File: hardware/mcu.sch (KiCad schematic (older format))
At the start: 17 parts

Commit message: przeniosiono do folderu hardware
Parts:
- added SW? (x2): SW_Push, symbol Switch:SW_Push
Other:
- note added: "or dip swichtes?\n"
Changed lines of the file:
@@
 Text Label 4900 4900 0    50   ~ 0
 POTSHDN
+$Comp
+L Switch:SW_Push SW?
+U 1 1 5D80555F
+P 8400 3600
+F 0 "SW?" H 8400 3885 50  0000 C CNN
+F 1 "SW_Push" H 8400 3794 50  0000 C CNN
+F 2 "" H 8400 3800 50  0001 C CNN
+F 3 "~" H 8400 3800 50  0001 C CNN
+	1    8400 3600
+	1    0    0    -1
+$EndComp
+$Comp
+L Switch:SW_Push SW?
+U 1 1 5D805DAF
+P 8400 4000
+F 0 "SW?" H 8400 4285 50  0000 C CNN
+F 1 "SW_Push" H 8400 4194 50  0000 C CNN
+F 2 "" H 8400 4200 50  0001 C CNN
+F 3 "~" H 8400 4200 50  0001 C CNN
+	1    8400 4000
+	1    0    0    -1
+$EndComp
+Text Notes 8100 3250 0    50   ~ 0
+or dip swichtes?\n
+Wire Notes Line
+	9200 4750 9200 2800
+Wire Notes Line
+	9200 2800 7800 2800
+Wire Notes Line
+	7800 2800 7800 4750
+Wire Notes Line
+	7800 4750 9200 4750
 $EndSCHEMATC

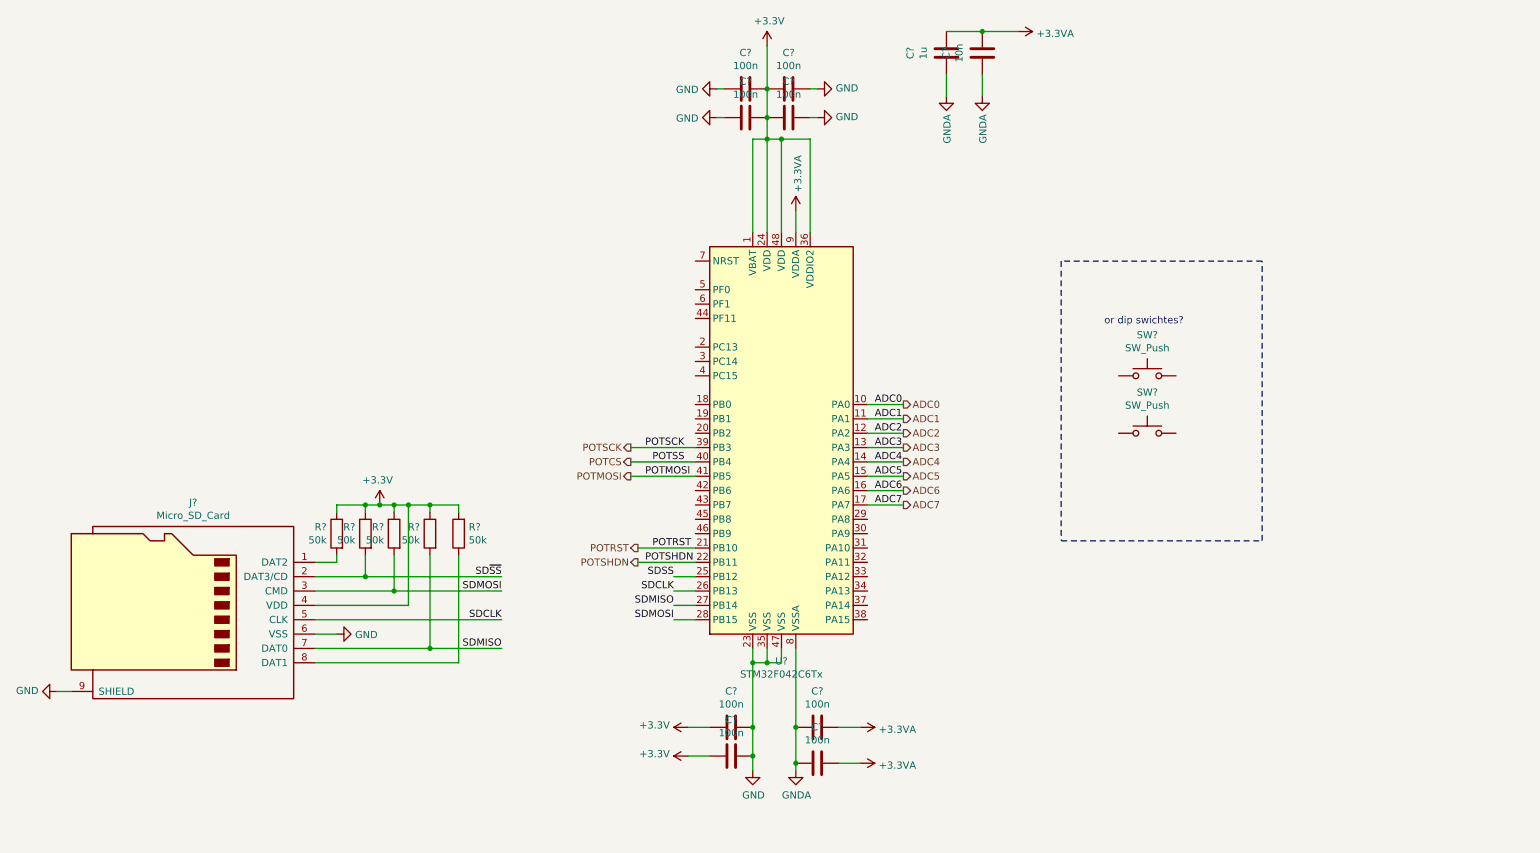
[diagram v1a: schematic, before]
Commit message: dodano wyjscie programatora, przyciski ustalono wysjcie i2c, dodany plik CubeMX z pinouterm
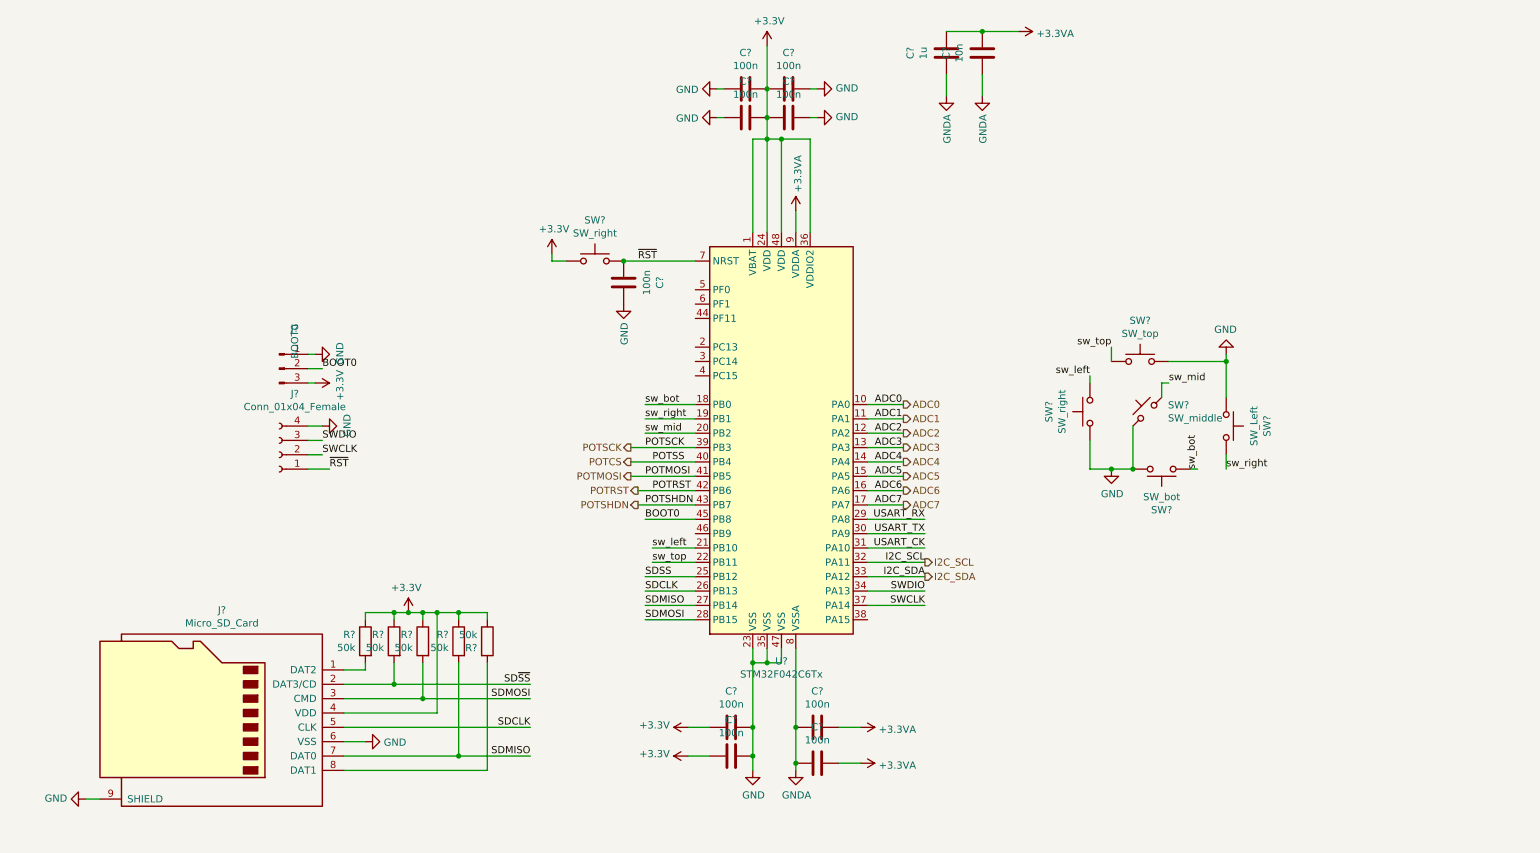
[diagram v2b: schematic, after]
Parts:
- added C?: 100n, symbol Device:C
- added J?: BOOT0, symbol Connector:Conn_01x03_Male
- added J?: Conn_01x04_Female, symbol Connector:Conn_01x04_Female
- added SW?: SW_top, symbol Switch:SW_Push
- added SW?: SW_bot, symbol Switch:SW_Push
- added SW?: SW_middle, symbol Switch:SW_Push_45deg
- added SW?: SW_right, symbol Switch:SW_Push
- SW?: value SW_Push -> SW_Left
- SW?: value SW_Push -> SW_right
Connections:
- net +3V3: now also R?.1, J?.3 (Pin_3), SW?.1; no longer R?.2
- net GND: now also SW?.1, SW?.1, C?.1, J?.1 (Pin_1), J?.4 (Pin_4), SW?.1, SW?.2, SW?.2
- net POTRST: now also U?.42 (PB6); no longer U?.21 (PB10)
- net POTSHDN: now also U?.43 (PB7); no longer U?.22 (PB11)
- net at J?.8 (DAT1): now also R?.2; no longer R?.1
- net sw_bot: now reaches U?.18 (PB0)
- net sw_bot: now also SW?.1
- net sw_right: now reaches U?.19 (PB1)
- net sw_right: now also SW?.2
- net sw_mid: now reaches U?.20 (PB2)
- net sw_mid: now also SW?.2
- net USART_RX: now reaches U?.29 (PA8)
- net USART_TX: now reaches U?.30 (PA9)
- net USART_CK: now reaches U?.31 (PA10)
- net I2C_SCL: now reaches U?.32 (PA11)
- net I2C_SDA: now reaches U?.33 (PA12)
- net SWDIO: now reaches U?.34 (PA13)
- net SWDIO: now also J?.3 (Pin_3)
- net SWCLK: now reaches U?.37 (PA14)
- net SWCLK: now also J?.2 (Pin_2)
- net BOOT0: now reaches U?.45 (PB8)
- net BOOT0: now also J?.2 (Pin_2)
- net ~RST: now reaches U?.7 (NRST)
- net ~RST: now also C?.2, J?.1 (Pin_1), SW?.2
- net sw_left: now reaches SW?.2
- net sw_left: now also U?.21 (PB10)
- new net sw_top: SW?.1, U?.22 (PB11)
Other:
- note removed: "or dip swichtes?\n"
- moved on the sheet: J?, R?, SW?

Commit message: DRC przechodzi dorzucone złącze do wyświetlacza na i2c oraz jeden push button
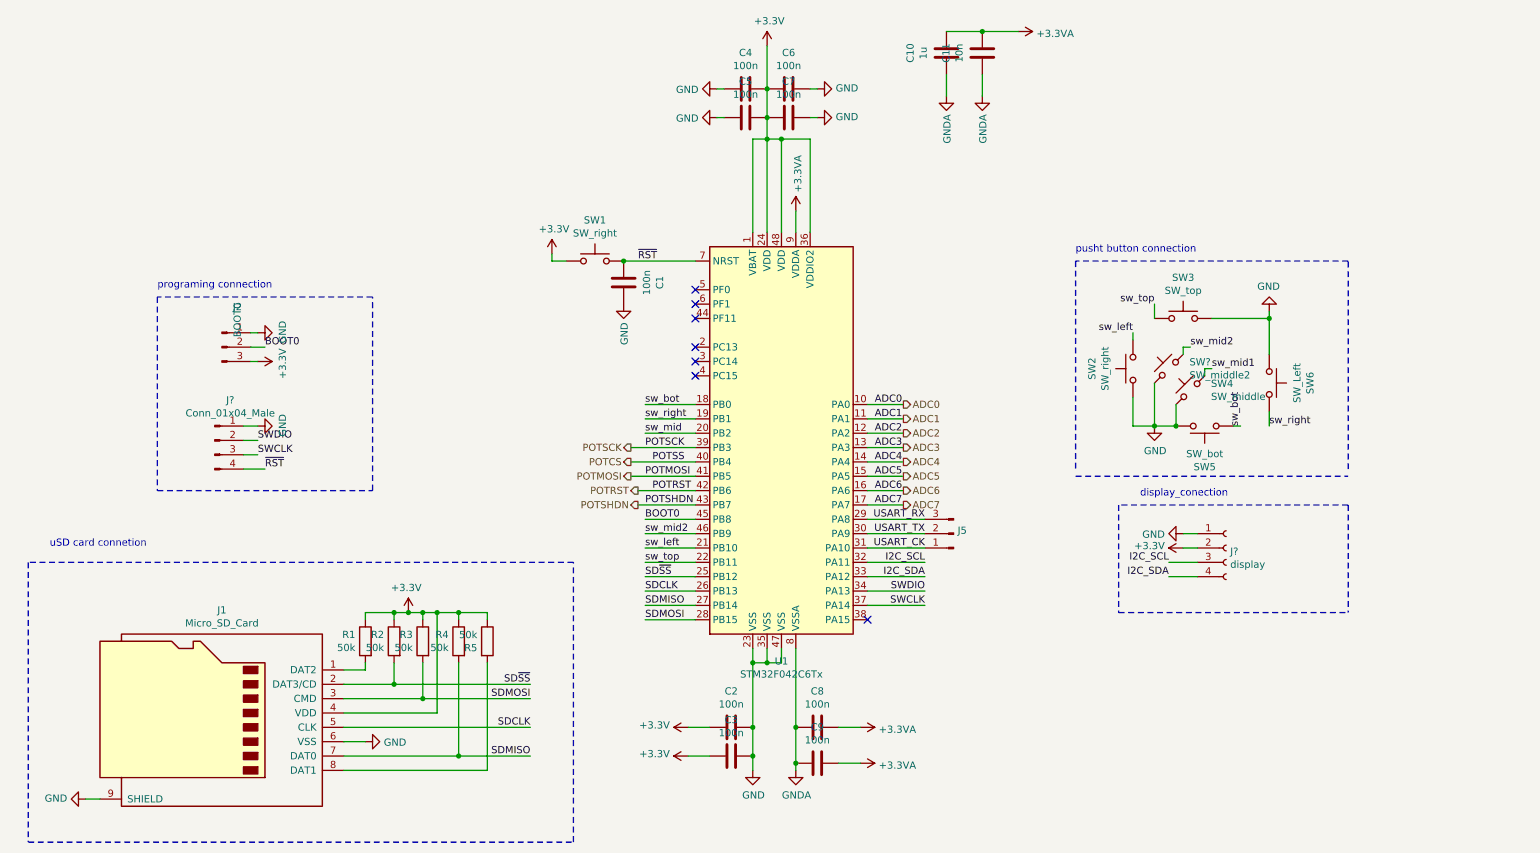
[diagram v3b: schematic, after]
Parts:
- removed J?: Conn_01x04_Female, symbol Connector:Conn_01x04_Female
- added J5: Conn_01x03_Male, symbol Connector:Conn_01x03_Male
- added J?: Conn_01x04_Male, symbol Connector:Conn_01x04_Male
- added J?: display, symbol Connector:Conn_01x04_Female
- added SW?: SW_middle2, symbol Switch:SW_Push_45deg
- gave numbers to parts that had none: 25
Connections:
- net SDSS is gone; now on net SD~SS: U1.25 (PB12)
- net +3V3: now also J?.2 (Pin_2)
- net GND: now also J?.1 (Pin_1), J?.1 (Pin_1), SW?.1
- net I2C_SCL: now also J?.3 (Pin_3)
- net I2C_SDA: now also J?.4 (Pin_4)
- net SWCLK: now also J?.3 (Pin_3)
- net SWDIO: now also J?.2 (Pin_2)
- net USART_CK: now also J5.1 (Pin_1)
- net USART_RX: now also J5.3 (Pin_3)
- net USART_TX: now also J5.2 (Pin_2)
- net sw_mid: no longer SW4.2
- net ~RST: now also J?.4 (Pin_4)
- net sw_mid2: now reaches U1.46 (PB9)
- net sw_mid2: now also SW?.2
- new net sw_mid1: SW4.2
- no-connect marks 0 -> 7
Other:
- note added: "display_conection"
- note added: "programing connection\n"
- note added: "pusht button connection"
- note added: "uSD card connetion\n"
- moved on the sheet: J2, SW2, SW3, SW4, SW5, SW6

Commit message: przypisano footprinty
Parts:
- C1, C10, C11, C2, C3, C4, C5, C6, C7, C8, C9: footprint (none) -> Capacitor_SMD:C_0603_1608Metric_Pad1.05x0.95mm_HandSolder
- J1: footprint (none) -> Connector_Card:microSD_HC_Hirose_DM3AT-SF-PEJM5
- J2: footprint (none) -> Connector_PinHeader_2.54mm:PinHeader_1x03_P2.54mm_Vertical
- J3: renamed from J?; footprint (none) -> Connector_PinHeader_2.54mm:PinHeader_1x04_P2.54mm_Vertical
- J5: footprint (none) -> Connector_PinHeader_2.54mm:PinHeader_1x03_P2.54mm_Horizontal
- J6: renamed from J?; footprint (none) -> Connector_PinSocket_2.54mm:PinSocket_1x04_P2.54mm_Vertical
- R1, R2, R3, R4, R5: footprint (none) -> Resistor_SMD:R_0603_1608Metric_Pad1.05x0.95mm_HandSolder
- SW1, SW2, SW3, SW4, SW5, SW6: footprint (none) -> Button_Switch_SMD:SW_Push_1P1T_NO_CK_KSC6xxJ
- SW7: renamed from SW?; footprint (none) -> Button_Switch_SMD:SW_Push_1P1T_NO_CK_KSC6xxJ
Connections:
- net sw_mid is gone; now on net sw_mid1: U1.20 (PB2)
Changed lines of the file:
@@
 F 0 "C2" V 5248 6050 50  0000 C CNN
 F 1 "100n" V 5339 6050 50  0000 C CNN
-F 2 "" H 5538 5900 50  0001 C CNN
+F 2 "Capacitor_SMD:C_0603_1608Metric_Pad1.05x0.95mm_HandSolder" H 5538 5900 50  0001 C CNN
 F 3 "~" H 5500 6050 50  0001 C CNN
 	1    5500 6050
@@
 F 0 "C6" V 5648 1600 50  0000 C CNN
 F 1 "100n" V 5739 1600 50  0000 C CNN
-F 2 "" H 5938 1450 50  0001 C CNN
+F 2 "Capacitor_SMD:C_0603_1608Metric_Pad1.05x0.95mm_HandSolder" H 5938 1450 50  0001 C CNN
 F 3 "~" H 5900 1600 50  0001 C CNN
 	1    5900 1600
@@
 F 0 "C7" V 5648 1800 50  0000 C CNN
 F 1 "100n" V 5739 1800 50  0000 C CNN
-F 2 "" H 5938 1650 50  0001 C CNN
+F 2 "Capacitor_SMD:C_0603_1608Metric_Pad1.05x0.95mm_HandSolder" H 5938 1650 50  0001 C CNN
 F 3 "~" H 5900 1800 50  0001 C CNN
 	1    5900 1800
@@
 F 0 "C4" V 5348 1600 50  0000 C CNN
 F 1 "100n" V 5439 1600 50  0000 C CNN
-F 2 "" H 5638 1450 50  0001 C CNN
+F 2 "Capacitor_SMD:C_0603_1608Metric_Pad1.05x0.95mm_HandSolder" H 5638 1450 50  0001 C CNN
 F 3 "~" H 5600 1600 50  0001 C CNN
 	1    5600 1600
@@
 F 0 "C5" V 5348 1800 50  0000 C CNN
 F 1 "100n" V 5439 1800 50  0000 C CNN
-F 2 "" H 5638 1650 50  0001 C CNN
+F 2 "Capacitor_SMD:C_0603_1608Metric_Pad1.05x0.95mm_HandSolder" H 5638 1650 50  0001 C CNN
 F 3 "~" H 5600 1800 50  0001 C CNN
 	1    5600 1800
@@
 F 0 "C11" V 6998 1350 50  0000 C CNN
 F 1 "10n" V 7089 1350 50  0000 C CNN
-F 2 "" H 7288 1200 50  0001 C CNN
+F 2 "Capacitor_SMD:C_0603_1608Metric_Pad1.05x0.95mm_HandSolder" H 7288 1200 50  0001 C CNN
 F 3 "~" H 7250 1350 50  0001 C CNN
 	1    7250 1350
@@
 F 0 "C10" V 6748 1350 50  0000 C CNN
 F 1 "1u" V 6839 1350 50  0000 C CNN
-F 2 "" H 7038 1200 50  0001 C CNN
+F 2 "Capacitor_SMD:C_0603_1608Metric_Pad1.05x0.95mm_HandSolder" H 7038 1200 50  0001 C CNN
 F 3 "~" H 7000 1350 50  0001 C CNN
 	1    7000 1350
@@
 F 0 "J1" H 1850 6667 50  0000 C CNN
 F 1 "Micro_SD_Card" H 1850 6576 50  0000 C CNN
-F 2 "" H 3050 6250 50  0001 C CNN
-F 3 "http://katalog.we-online.de/em/datasheet/693072010801.pdf" H 1900 5950 50  0001 C CNN
+F 2 "Connector_Card:microSD_HC_Hirose_DM3AT-SF-PEJM5" H 3050 6250 50  0001 C CNN
+F 3 "https://www.tme.eu/pl/details/mcsp-q-08-a-sg/zlacza-do-kart/adam-tech/mcsp-q-08-a-sg-t-r/" H 1900 5950 50  0001 C CNN
 	1    1900 5950
 	-1   0    0    -1
@@
 F 0 "R1" H 3020 5496 50  0000 L CNN
 F 1 "50k" H 3020 5405 50  0000 L CNN
-F 2 "" V 2880 5450 50  0001 C CNN
+F 2 "Resistor_SMD:R_0603_1608Metric_Pad1.05x0.95mm_HandSolder" V 2880 5450 50  0001 C CNN
 F 3 "~" H 2950 5450 50  0001 C CNN
 	1    2950 5450
@@
 F 0 "R2" H 3220 5496 50  0000 L CNN
 F 1 "50k" H 3220 5405 50  0000 L CNN
-F 2 "" V 3080 5450 50  0001 C CNN
+F 2 "Resistor_SMD:R_0603_1608Metric_Pad1.05x0.95mm_HandSolder" V 3080 5450 50  0001 C CNN
 F 3 "~" H 3150 5450 50  0001 C CNN
 	1    3150 5450
@@
 F 0 "R3" H 3420 5496 50  0000 L CNN
 F 1 "50k" H 3420 5405 50  0000 L CNN
-F 2 "" V 3280 5450 50  0001 C CNN
+F 2 "Resistor_SMD:R_0603_1608Metric_Pad1.05x0.95mm_HandSolder" V 3280 5450 50  0001 C CNN
 F 3 "~" H 3350 5450 50  0001 C CNN
 	1    3350 5450
@@
 F 0 "R4" H 3670 5496 50  0000 L CNN
 F 1 "50k" H 3670 5405 50  0000 L CNN
-F 2 "" V 3530 5450 50  0001 C CNN
+F 2 "Resistor_SMD:R_0603_1608Metric_Pad1.05x0.95mm_HandSolder" V 3530 5450 50  0001 C CNN
 F 3 "~" H 3600 5450 50  0001 C CNN
 	1    3600 5450
@@
 F 0 "R5" H 3730 5404 50  0000 R CNN
 F 1 "50k" H 3730 5495 50  0000 R CNN
-F 2 "" V 3730 5450 50  0001 C CNN
+F 2 "Resistor_SMD:R_0603_1608Metric_Pad1.05x0.95mm_HandSolder" V 3730 5450 50  0001 C CNN
 F 3 "~" H 3800 5450 50  0001 C CNN
 	1    3800 5450
@@
 F 0 "C3" V 5248 6250 50  0000 C CNN
 F 1 "100n" V 5339 6250 50  0000 C CNN
-F 2 "" H 5538 6100 50  0001 C CNN
+F 2 "Capacitor_SMD:C_0603_1608Metric_Pad1.05x0.95mm_HandSolder" H 5538 6100 50  0001 C CNN
 F 3 "~" H 5500 6250 50  0001 C CNN
 	1    5500 6250
@@
 F 0 "C8" V 5848 6050 50  0000 C CNN
 F 1 "100n" V 5939 6050 50  0000 C CNN
-F 2 "" H 6138 5900 50  0001 C CNN
+F 2 "Capacitor_SMD:C_0603_1608Metric_Pad1.05x0.95mm_HandSolder" H 6138 5900 50  0001 C CNN
 F 3 "~" H 6100 6050 50  0001 C CNN
 	1    6100 6050
@@
 F 0 "C9" V 5848 6300 50  0000 C CNN
 F 1 "100n" V 5939 6300 50  0000 C CNN
-F 2 "" H 6138 6150 50  0001 C CNN
+F 2 "Capacitor_SMD:C_0603_1608Metric_Pad1.05x0.95mm_HandSolder" H 6138 6150 50  0001 C CNN
 F 3 "~" H 6100 6300 50  0001 C CNN
 	1    6100 6300
@@
 F 0 "SW6" H 9250 3935 50  0000 C CNN
 F 1 "SW_Left" H 9250 3844 50  0000 C CNN
-F 2 "" H 9250 3850 50  0001 C CNN
+F 2 "Button_Switch_SMD:SW_Push_1P1T_NO_CK_KSC6xxJ" H 9250 3850 50  0001 C CNN
 F 3 "~" H 9250 3850 50  0001 C CNN
 	1    9250 3650
@@
 F 0 "SW2" H 8300 3835 50  0000 C CNN
 F 1 "SW_right" H 8300 3744 50  0000 C CNN
-F 2 "" H 8300 3750 50  0001 C CNN
+F 2 "Button_Switch_SMD:SW_Push_1P1T_NO_CK_KSC6xxJ" H 8300 3750 50  0001 C CNN
 F 3 "~" H 8300 3750 50  0001 C CNN
 	1    8300 3550
@@
 F 0 "SW3" H 8650 3485 50  0000 C CNN
 F 1 "SW_top" H 8650 3394 50  0000 C CNN
-F 2 "" H 8650 3400 50  0001 C CNN
+F 2 "Button_Switch_SMD:SW_Push_1P1T_NO_CK_KSC6xxJ" H 8650 3400 50  0001 C CNN
 F 3 "~" H 8650 3400 50  0001 C CNN
 	1    8650 3200
@@
 F 0 "SW5" H 8800 4235 50  0000 C CNN
 F 1 "SW_bot" H 8800 4144 50  0000 C CNN
-F 2 "" H 8800 4150 50  0001 C CNN
+F 2 "Button_Switch_SMD:SW_Push_1P1T_NO_CK_KSC6xxJ" H 8800 4150 50  0001 C CNN
 F 3 "~" H 8800 4150 50  0001 C CNN
 	1    8800 3950
@@
 F 0 "SW4" V 8746 3556 50  0000 R CNN
 F 1 "SW_middle" V 8655 3556 50  0000 R CNN
-F 2 "" H 8700 3700 50  0001 C CNN
+F 2 "Button_Switch_SMD:SW_Push_1P1T_NO_CK_KSC6xxJ" H 8700 3700 50  0001 C CNN
 F 3 "~" H 8700 3700 50  0001 C CNN
 	1    8700 3700
@@
 sw_left
 Text Label 4900 4000 0    50   ~ 0
-sw_mid
+sw_mid1
 Text Label 4900 3900 0    50   ~ 0
 sw_right
@@
 F 0 "C1" V 4498 2950 50  0000 C CNN
 F 1 "100n" V 4589 2950 50  0000 C CNN
-F 2 "" H 4788 2800 50  0001 C CNN
+F 2 "Capacitor_SMD:C_0603_1608Metric_Pad1.05x0.95mm_HandSolder" H 4788 2800 50  0001 C CNN
 F 3 "~" H 4750 2950 50  0001 C CNN
 	1    4750 2950
@@
 F 0 "J2" H 2058 3681 50  0000 C CNN
 F 1 "BOOT0" V 2058 3590 50  0000 C CNN
-F 2 "" H 1950 3400 50  0001 C CNN
+F 2 "Connector_PinHeader_2.54mm:PinHeader_1x03_P2.54mm_Vertical" H 1950 3400 50  0001 C CNN
 F 3 "~" H 1950 3400 50  0001 C CNN
 	1    1950 3400
@@
 F 0 "SW1" H 4550 3085 50  0000 C CNN
 F 1 "SW_right" H 4550 2994 50  0000 C CNN
-F 2 "" H 4550 3000 50  0001 C CNN
+F 2 "Button_Switch_SMD:SW_Push_1P1T_NO_CK_KSC6xxJ" H 4550 3000 50  0001 C CNN
 F 3 "~" H 4550 3000 50  0001 C CNN
 	1    4550 2800
@@
 F 0 "J5" H 7022 4678 50  0000 R CNN
 F 1 "Conn_01x03_Male" H 7158 4890 50  0001 C CNN
-F 2 "" H 7050 4700 50  0001 C CNN
+F 2 "Connector_PinHeader_2.54mm:PinHeader_1x03_P2.54mm_Horizontal" H 7050 4700 50  0001 C CNN
 F 3 "~" H 7050 4700 50  0001 C CNN
 	1    7050 4700
@@
 I2C_SDA
 $Comp
-L Connector:Conn_01x04_Male J?
+L Connector:Conn_01x04_Male J3
 U 1 1 5D24AFE9
 P 1900 4050
-F 0 "J?" H 2008 4331 50  0000 C CNN
+F 0 "J3" H 2008 4331 50  0000 C CNN
 F 1 "Conn_01x04_Male" H 2008 4240 50  0000 C CNN
-F 2 "" H 1900 4050 50  0001 C CNN
+F 2 "Connector_PinHeader_2.54mm:PinHeader_1x04_P2.54mm_Vertical" H 1900 4050 50  0001 C CNN
 F 3 "~" H 1900 4050 50  0001 C CNN
 	1    1900 4050
@@
 $EndComp
 $Comp
-L Connector:Conn_01x04_Female J?
+L Connector:Conn_01x04_Female J6
 U 1 1 5D24C80E
 P 8950 4800
-F 0 "J?" H 8978 4776 50  0000 L CNN
+F 0 "J6" H 8978 4776 50  0000 L CNN
 F 1 "display" H 8978 4685 50  0000 L CNN
-F 2 "" H 8950 4800 50  0001 C CNN
+F 2 "Connector_PinSocket_2.54mm:PinSocket_1x04_P2.54mm_Vertical" H 8950 4800 50  0001 C CNN
 F 3 "~" H 8950 4800 50  0001 C CNN
 	1    8950 4800
@@
 	9800 4500 9800 5250
 $Comp
-L Switch:SW_Push_45deg SW?
+L Switch:SW_Push_45deg SW7
 U 1 1 5D29299F
 P 8550 3550
-F 0 "SW?" V 8596 3406 50  0000 R CNN
+F 0 "SW7" V 8596 3406 50  0000 R CNN
 F 1 "SW_middle2" V 8505 3406 50  0000 R CNN
-F 2 "" H 8550 3550 50  0001 C CNN
+F 2 "Button_Switch_SMD:SW_Push_1P1T_NO_CK_KSC6xxJ" H 8550 3550 50  0001 C CNN
 F 3 "~" H 8550 3550 50  0001 C CNN
 	1    8550 3550
